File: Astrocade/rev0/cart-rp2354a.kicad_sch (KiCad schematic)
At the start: 44 parts, among them J1 Astrocade_Cart_Edge_26, SW1 RESET, SW2 BOOTSEL, U1 RP2354A, Y1 12MHz

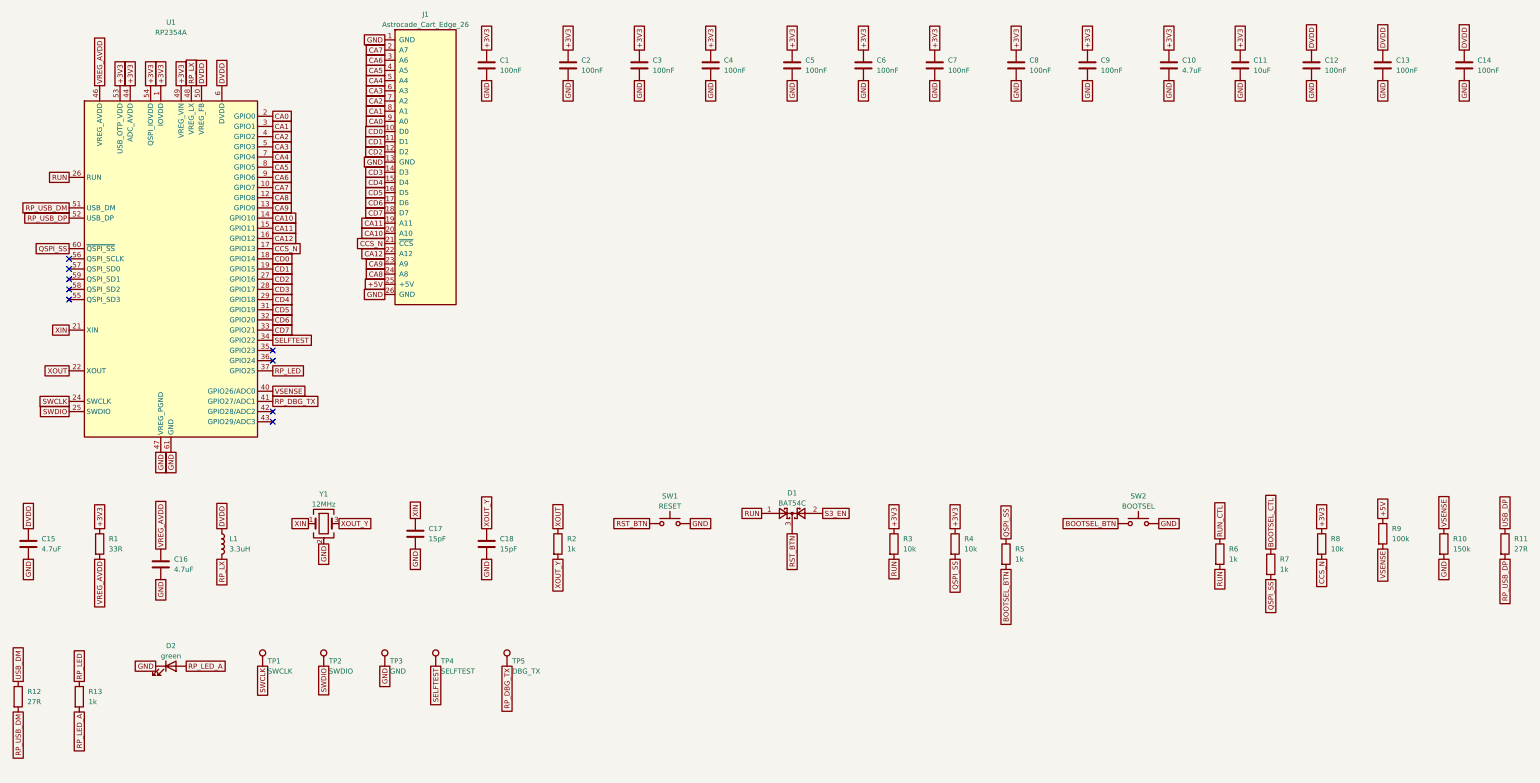
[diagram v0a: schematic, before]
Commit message: Astrocade Rev0: audit with kicad-happy + datasheets and redo
Schematic, board and fab outputs regenerated from tools/ after a
datasheet-level audit (docs/design-review-rev0.md).

Design fixes:
- RP2354A on its own AP2112K rail (+3V3_RP): its FT pads take 5.5 V only
  with IOVDD powered (RP2350 DS p.1332); the buck's UVLO + 4 ms soft-start
  left them unpowered while the console drove the bus
- WS2812B-2020-V6 on +5V (datasheet VDD 3.7-5.3 V, not a 3.3 V part)
- VBUS decoupling at the USB-C, activity LED 330R, card-detect polarity
  settled (low = card present), fiducials, RUN/BOOTSEL/rail test pads

Schematic redrawn readably: root block diagram with hierarchical pins,
power symbols, wired clusters and design notes (tools/sch_layout.py);
check_sch_layout.py proves the drawn netlist equals design.py.

Board: 4 layers tried first and did not close; 6 layers, 100% routed,
DRC 0 errors / 0 unconnected / 0 parity. Locked USB-C D+/D- pad ties,
GND stitching kept out of pads, return vias at USB/crystal layer
changes, check_vias.py gate (KiCad re-nets a via inside another net's
pad, so its DRC cannot see it).

Co-Authored-By: Claude Opus 5.5 <noreply@anthropic.com>
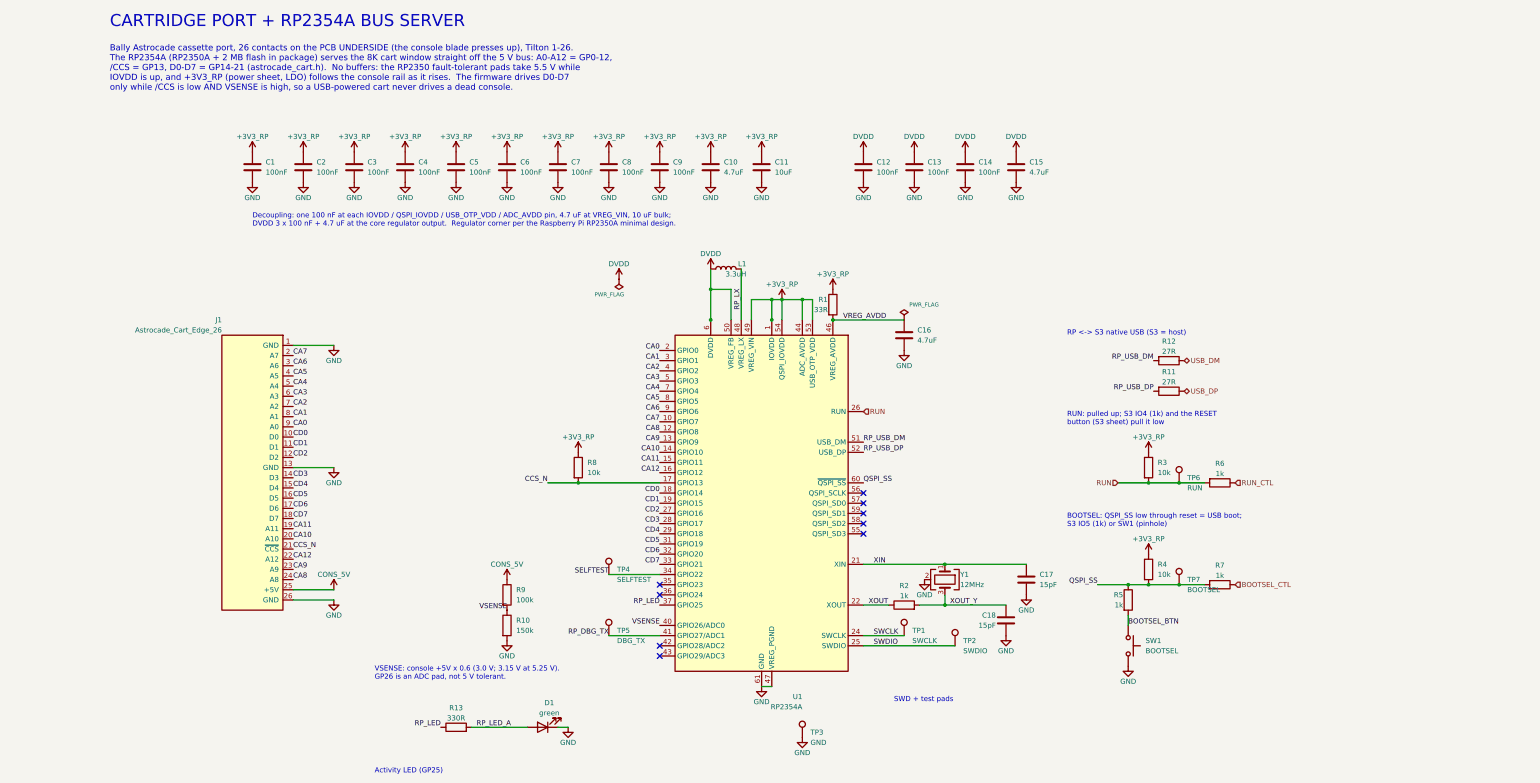
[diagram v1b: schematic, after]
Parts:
- removed D2: green, FujiNet-Astrocade:LED_0603_1608Metric, symbol Device:LED
- removed SW2: BOOTSEL, FujiNet-Astrocade:SW_SPST_TL3342, symbol Switch:SW_Push
- added TP6: RUN, FujiNet-Astrocade:TestPoint_Pad_D1.5mm, symbol Connector:TestPoint
- added TP7: BOOTSEL, FujiNet-Astrocade:TestPoint_Pad_D1.5mm, symbol Connector:TestPoint
- D1: value BAT54C -> green; footprint FujiNet-Astrocade:SOT-23 -> FujiNet-Astrocade:LED_0603_1608Metric; symbol Diode:BAT54C -> Device:LED; LCSC C37704 -> C12624; MPN BAT54C,215 -> KT-0603G
- R13: value 1k -> 330R; LCSC C21190 -> C23138; MPN 0603WAF1001T5E -> 0603WAF3300T5E
- SW1: value RESET -> BOOTSEL
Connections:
- net S3_EN is gone; now on net RP_LED_A: D1.2 (A)
- net BOOTSEL_BTN: now also SW1.1
- net GND: now also D1.1 (K)
- net QSPI_SS: now also TP7.1
- net RUN: now also TP6.1; no longer D1.1
- net +3V3 renamed +3V3_RP
- net +5V renamed CONS_5V
- removed net RST_BTN: D1.3, SW1.1
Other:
- note added: "Activity LED (GP25)"
- note added: "BOOTSEL: QSPI_SS low through reset = USB boot; S3 IO5 (1k) or SW1 (pinhole)"
- note added: "Bally Astrocade cassette port, 26 contacts on the PCB UNDERSIDE (the console blade presses up), Tilton 1-26. The RP2354A (RP2350A + 2 MB flash in package) serves the 8K cart window straight off the 5 V bus: A0-A12 = GP0-12, /CCS = GP13, D0-D7 = GP14-21 (astrocade_cart.h). No buffers: the RP2350 fault-tolerant pads take 5.5 V while IOVDD is up, and +3V3_RP (power sheet, LDO) follows the console ra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"
- note added: "CARTRIDGE PORT + RP2354A BUS SERVER"
- note added: "Decoupling: one 100 nF at each IOVDD / QSPI_IOVDD / USB_OTP_VDD / ADC_AVDD pin, 4.7 uF at VREG_VIN, 10 uF bulk; DVDD 3 x 100 nF + 4.7 uF at the core regulator output. Regulator corner per the Raspberry Pi RP2350A minimal design."
- note added: "RP <-> S3 native USB (S3 = host)"
- note added: "RUN: pulled up; S3 IO4 (1k) and the RESET button (S3 sheet) pull it low"
- note added: "SWD + test pads"
- note added: "VSENSE: console +5V x 0.6 (3.0 V; 3.15 V at 5.25 V). GP26 is an ADC pad, not 5 V tolerant."
- title: FujiNet Astrocade Rev0 - RP2354A cartridge bus controller + edge -> FujiNet Astrocade Rev0 - Cartridge port + RP2354A bus server
- moved on the sheet: C1, C10, C11, C12, C13, C14, C15, C16, C17, C18, C2, C3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
